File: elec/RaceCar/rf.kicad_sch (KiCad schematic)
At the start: 1 part, among them U1 MICRF220AYQS

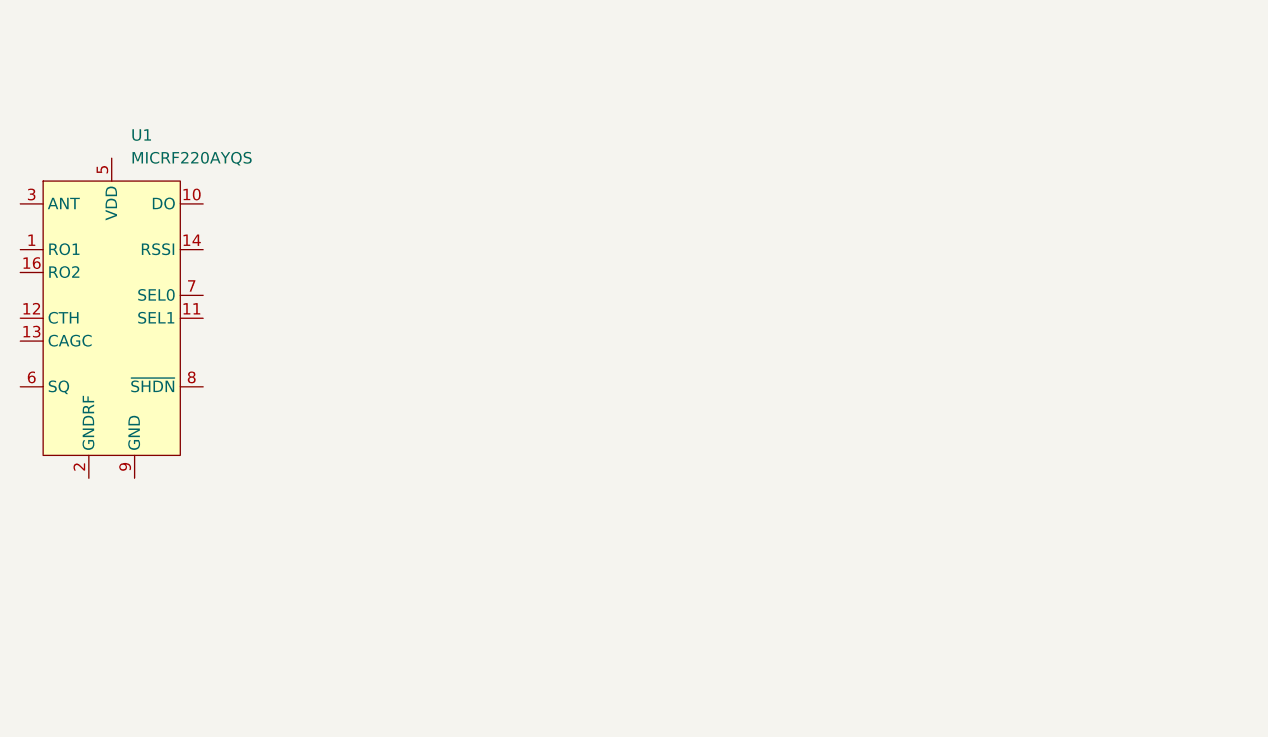
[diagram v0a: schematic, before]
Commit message: Ajout du rx
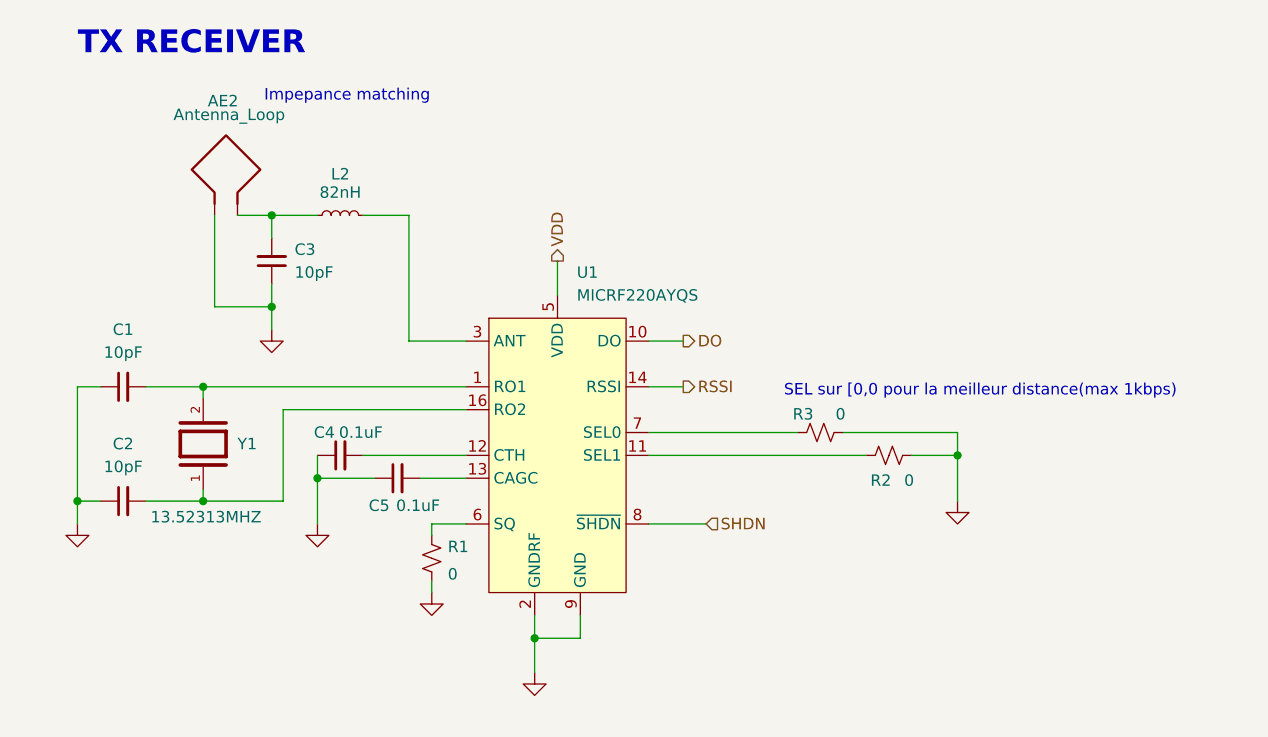
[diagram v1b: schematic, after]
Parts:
- added AE2: Antenna_Loop, symbol Device:Antenna_Loop
- added C1, C2, C3: 10pF, Capacitor_SMD:C_0603_1608Metric, symbol Device:C_Small
- added C4, C5: 0.1uF, Capacitor_SMD:C_0603_1608Metric, symbol Device:C_Small
- added L2: 82nH, Inductor_SMD:L_0603_1608Metric, symbol Device:L_Small
- added R1, R2, R3: 0, Resistor_SMD:R_0603_1608Metric, symbol Device:R_Small_US
- added Y1: 13.52313MHZ, $C3I:XTAL_ABM3-13.52313MHZ-10-B4Y-T, symbol $C3I:ABM3-13.52313MHZ-10-B4Y-T
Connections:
- net at U1.1 (RO1): now also C1.2, Y1.2
- net DO: now reaches U1.10 (DO)
- net at U1.11 (SEL1): now also R2.1
- net at U1.12 (CTH): now also C4.2
- net at U1.13 (CAGC): now also C5.2
- net RSSI: now reaches U1.14 (RSSI)
- net at U1.16 (RO2): now also C2.2, Y1.1
- net GND: now reaches U1.2 (GNDRF), U1.4 (GNDRF)
- net GND: now also U1.9 (GND), AE2.1, C1.1, C2.1, C3.1, C4.1, C5.1, R1.2, R2.2, R3.2
- net at U1.3 (ANT): now also L2.2
- net VDD: now reaches U1.5 (VDD)
- net at U1.6 (SQ): now also R1.1
- net at U1.7 (SEL0): now also R3.1
- net SHDN: now reaches U1.8 (~{SHDN})
- new net: AE2.2, C3.2, L2.1
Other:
- note added: "Impepance matching"
- note added: "SEL sur [0,0 pour la meilleur distance(max 1kbps)"
- note added: "TX RECEIVER"
- moved on the sheet: U1

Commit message: Ajout du power et du stm
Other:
- note added: "RX RECEIVER"
- note removed: "TX RECEIVER"
